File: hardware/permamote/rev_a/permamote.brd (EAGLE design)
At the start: 27 x 60 mm, 131 parts, among them J1 TC2030-JLINK-NL, J5 MICRO_USB_B_HIROSE_ZX62R-B-5P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, Q1 PMDXB950UPEL, Q10 PMDXB950UPEL, Q2 PMDXB950UPEL, Q3 PMDXB950UPEL, Q4 PMDXB950UPEL, Q5 PMDXB950UPEL, Q6 PMDXB950UPEL, Q7 PMDXB950UPEL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

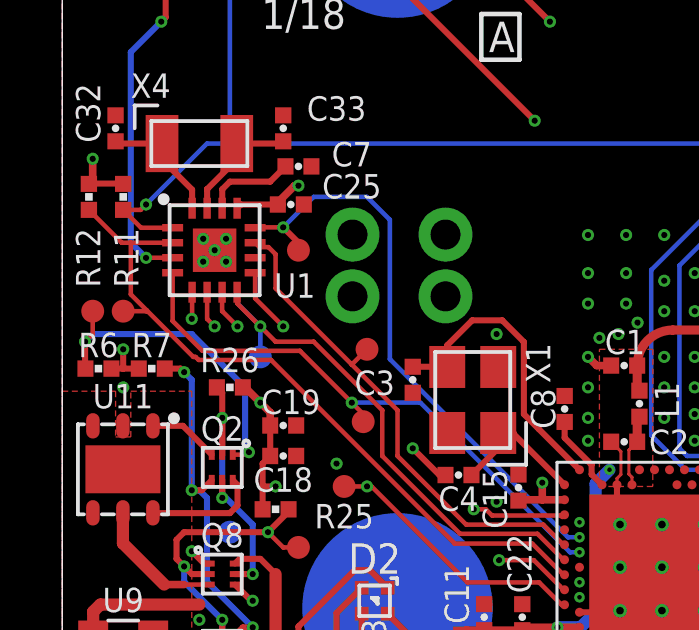
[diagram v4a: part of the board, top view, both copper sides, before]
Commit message: Fix orphaned trace
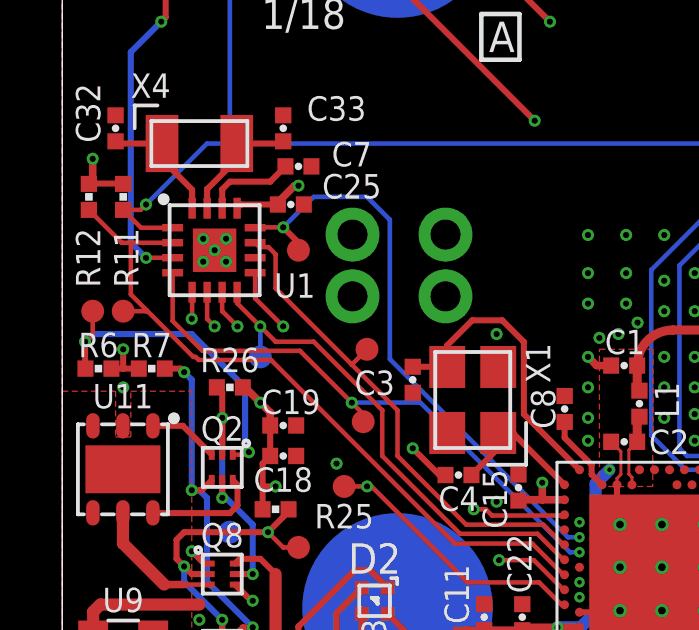
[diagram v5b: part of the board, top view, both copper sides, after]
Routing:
- net !RTC_IRQ3: track 17.8 -> 16.7 mm
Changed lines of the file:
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@@
 <wire x1="10.668" y1="20.32" x2="10.668" y2="21.844" width="0.1524" layer="1"/>
 <via x="6.604" y="24.638" extent="1-16" drill="0.2032"/>
-<wire x1="5.842" y1="25.4" x2="6.604" y2="24.638" width="0.1524" layer="16"/>
 <wire x1="8.382" y1="24.13" x2="7.112" y2="24.13" width="0.1524" layer="1"/>
 <wire x1="7.112" y1="24.13" x2="6.604" y2="24.638" width="0.1524" layer="1"/>
